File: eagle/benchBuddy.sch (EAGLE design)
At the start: 104 parts, among them IC2 TLC274D, IC3 LM334Z, IC4 LM324D, IC5 LM324D, J1 12V_DC, J2 PHOENIX_SPRING_TERM_2POS, J4 GND, J5 3.3V, J6 5V, J7 12V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

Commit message: Power jack changed
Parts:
- removed J1: 12V_DC, SparkFun-Connectors:POWER_JACKSLT
- added J10: (no value), con-jack:JACK-PLUG1
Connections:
- net GND: now also J10.1, J10.2; no longer J1.GND, J1.GNDBREAK
- net N$3: now also J10.3; no longer J1.PWR
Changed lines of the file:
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@@
 <part name="SUPPLY1" library="SparkFun-PowerSymbols" library_urn="urn:adsk.eagle:library:530" deviceset="VIN" device=""/>
 <part name="P+1" library="supply1" library_urn="urn:adsk.eagle:library:371" deviceset="VCC" device=""/>
-<part name="J1" library="SparkFun-Connectors" library_urn="urn:adsk.eagle:library:513" deviceset="POWER_JACK" device="SLT" package3d_urn="urn:adsk.eagle:package:38222/1" value="12V_DC"/>
 <part name="IC2" library="linear" library_urn="urn:adsk.eagle:library:262" deviceset="TLC274" device="D" package3d_urn="urn:adsk.eagle:package:16406/2"/>
 <part name="IC3" library="linear" library_urn="urn:adsk.eagle:library:262" deviceset="LM*34" device="Z" package3d_urn="urn:adsk.eagle:package:16416/2" technology="3"/>
@@
 <part name="H5" library="holes" library_urn="urn:adsk.eagle:library:237" deviceset="MOUNT-HOLE" device="2.8" package3d_urn="urn:adsk.eagle:package:14271/1"/>
 <part name="H6" library="holes" library_urn="urn:adsk.eagle:library:237" deviceset="MOUNT-HOLE" device="2.8" package3d_urn="urn:adsk.eagle:package:14271/1"/>
+<part name="J10" library="con-jack" library_urn="urn:adsk.eagle:library:154" deviceset="JACK-PLUG" device="1" package3d_urn="urn:adsk.eagle:package:7494/1"/>
 </parts>
 <sheets>
@@
 <attribute name="VALUE" x="236.22" y="187.96" size="1.778" layer="96" rot="R90"/>
 </instance>
-<instance part="J1" gate="G$1" x="17.78" y="177.8" smashed="yes">
-<attribute name="VALUE" x="7.62" y="187.96" size="1.778" layer="96" font="vector"/>
-<attribute name="NAME" x="7.62" y="177.8" size="1.778" layer="95" font="vector"/>
-</instance>
 <instance part="IC2" gate="A" x="172.72" y="119.38" smashed="yes">
 <attribute name="NAME" x="175.26" y="122.555" size="1.778" layer="95"/>
@@
 <attribute name="VALUE" x="151.892" y="22.9362" size="1.778" layer="96"/>
 </instance>
+<instance part="J10" gate="G$1" x="15.24" y="182.88"/>
 </instances>
 <busses>
@@
 <segment>
 <pinref part="GND1" gate="1" pin="GND"/>
-<pinref part="J1" gate="G$1" pin="GND"/>
 <wire x1="33.02" y1="175.26" x2="33.02" y2="180.34" width="0.1524" layer="91"/>
 <wire x1="33.02" y1="180.34" x2="20.32" y2="180.34" width="0.1524" layer="91"/>
-<pinref part="J1" gate="G$1" pin="GNDBREAK"/>
-<wire x1="20.32" y1="182.88" x2="33.02" y2="182.88" width="0.1524" layer="91"/>
 <wire x1="33.02" y1="182.88" x2="33.02" y2="180.34" width="0.1524" layer="91"/>
 <junction x="33.02" y="180.34"/>
+<pinref part="J10" gate="G$1" pin="1"/>
+<pinref part="J10" gate="G$1" pin="2"/>
+<wire x1="20.32" y1="182.88" x2="33.02" y2="182.88" width="0.1524" layer="91"/>
 </segment>
 <segment>
@@
 </segment>
 </net>
-<net name="N$3" class="0">
-<segment>
-<pinref part="F1" gate="G$1" pin="P$1"/>
-<pinref part="J1" gate="G$1" pin="PWR"/>
-<wire x1="22.86" y1="185.42" x2="20.32" y2="185.42" width="0.1524" layer="91"/>
-</segment>
-</net>
 <net name="N$44" class="0">
 <segment>
@@
 </segment>
 </net>
+<net name="N$3" class="0">
+<segment>
+<pinref part="F1" gate="G$1" pin="P$1"/>
+<pinref part="J10" gate="G$1" pin="3"/>
+<wire x1="22.86" y1="185.42" x2="20.32" y2="185.42" width="0.1524" layer="91"/>
+</segment>
+</net>

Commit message: Changed jack, again
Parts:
- J10: device con-jack:JACK-PLUG1 -> con-jack:JACK-PLUG0
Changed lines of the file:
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@@
 <part name="H5" library="holes" library_urn="urn:adsk.eagle:library:237" deviceset="MOUNT-HOLE" device="2.8" package3d_urn="urn:adsk.eagle:package:14271/1"/>
 <part name="H6" library="holes" library_urn="urn:adsk.eagle:library:237" deviceset="MOUNT-HOLE" device="2.8" package3d_urn="urn:adsk.eagle:package:14271/1"/>
-<part name="J10" library="con-jack" library_urn="urn:adsk.eagle:library:154" deviceset="JACK-PLUG" device="1" package3d_urn="urn:adsk.eagle:package:7494/1"/>
+<part name="J10" library="con-jack" library_urn="urn:adsk.eagle:library:154" deviceset="JACK-PLUG" device="0" package3d_urn="urn:adsk.eagle:package:7492/1"/>
 </parts>
 <sheets>
@@
 <attribute name="VALUE" x="151.892" y="22.9362" size="1.778" layer="96"/>
 </instance>
-<instance part="J10" gate="G$1" x="15.24" y="182.88"/>
+<instance part="J10" gate="G$1" x="15.24" y="182.88" smashed="yes">
+<attribute name="NAME" x="7.62" y="187.96" size="1.778" layer="95"/>
+<attribute name="VALUE" x="7.62" y="177.8" size="1.778" layer="96"/>
+</instance>
 </instances>
 <busses>

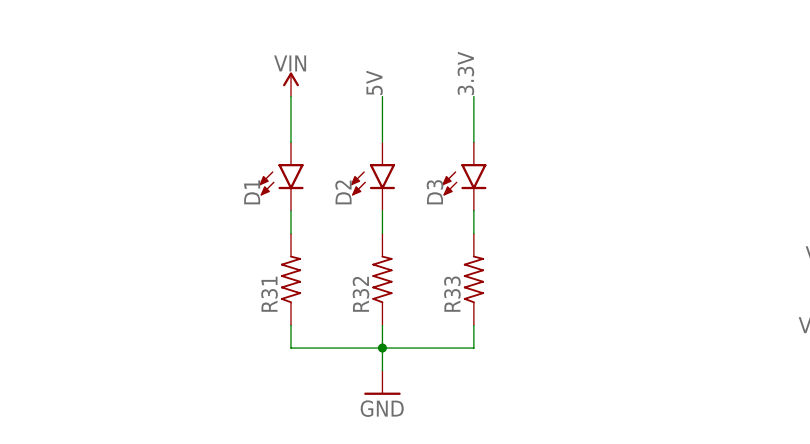
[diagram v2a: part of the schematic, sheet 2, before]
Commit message: worked on BOM. Added values to LED resistors.
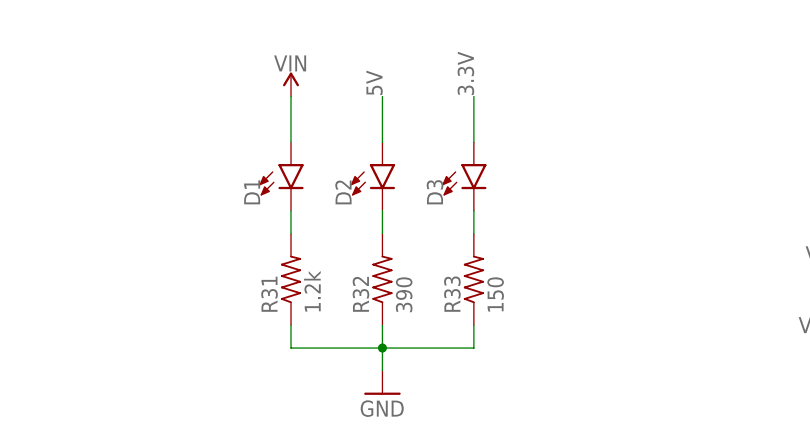
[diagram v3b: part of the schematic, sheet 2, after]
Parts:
- R31: value (none) -> 1.2k
- R32: value (none) -> 390
- R33: value (none) -> 150
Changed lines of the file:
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@@
 <part name="D3" library="SparkFun-LED" library_urn="urn:adsk.eagle:library:529" deviceset="LED" device="3MM" package3d_urn="urn:adsk.eagle:package:39361/1"/>
 <part name="U3" library="lab07lib" deviceset="3V3REG" device="-HEATSINK"/>
-<part name="R31" library="rcl" library_urn="urn:adsk.eagle:library:334" deviceset="R-US_" device="R1206" package3d_urn="urn:adsk.eagle:package:23540/2"/>
-<part name="R32" library="rcl" library_urn="urn:adsk.eagle:library:334" deviceset="R-US_" device="R1206" package3d_urn="urn:adsk.eagle:package:23540/2"/>
-<part name="R33" library="rcl" library_urn="urn:adsk.eagle:library:334" deviceset="R-US_" device="R1206" package3d_urn="urn:adsk.eagle:package:23540/2"/>
+<part name="R31" library="rcl" library_urn="urn:adsk.eagle:library:334" deviceset="R-US_" device="R1206" package3d_urn="urn:adsk.eagle:package:23540/2" value="1.2k"/>
+<part name="R32" library="rcl" library_urn="urn:adsk.eagle:library:334" deviceset="R-US_" device="R1206" package3d_urn="urn:adsk.eagle:package:23540/2" value="390"/>
+<part name="R33" library="rcl" library_urn="urn:adsk.eagle:library:334" deviceset="R-US_" device="R1206" package3d_urn="urn:adsk.eagle:package:23540/2" value="150"/>
 <part name="GND23" library="supply1" library_urn="urn:adsk.eagle:library:371" deviceset="GND" device=""/>
 <part name="GND24" library="supply1" library_urn="urn:adsk.eagle:library:371" deviceset="GND" device=""/>
